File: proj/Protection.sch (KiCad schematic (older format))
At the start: 18 parts

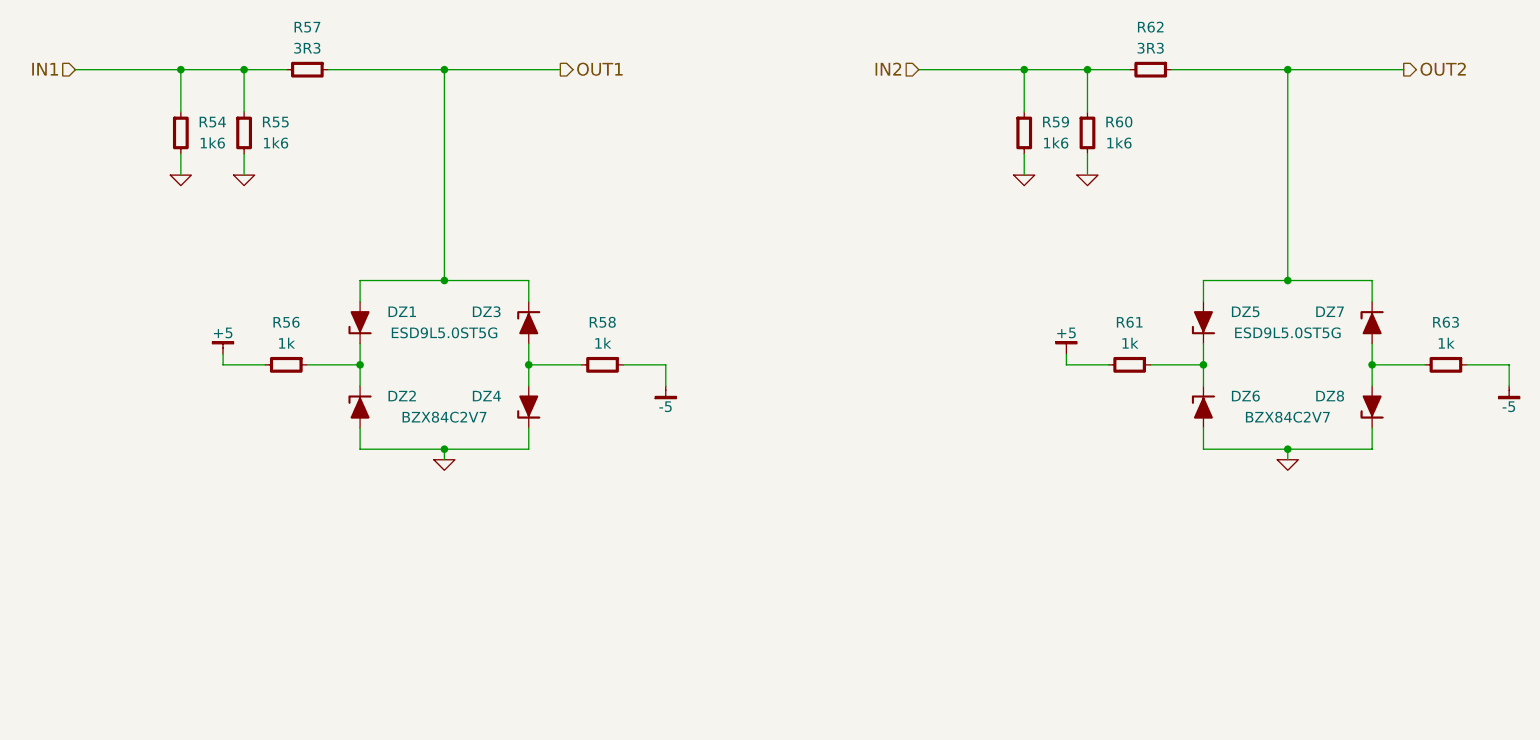
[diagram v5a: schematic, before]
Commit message: Clean up resistor BOM
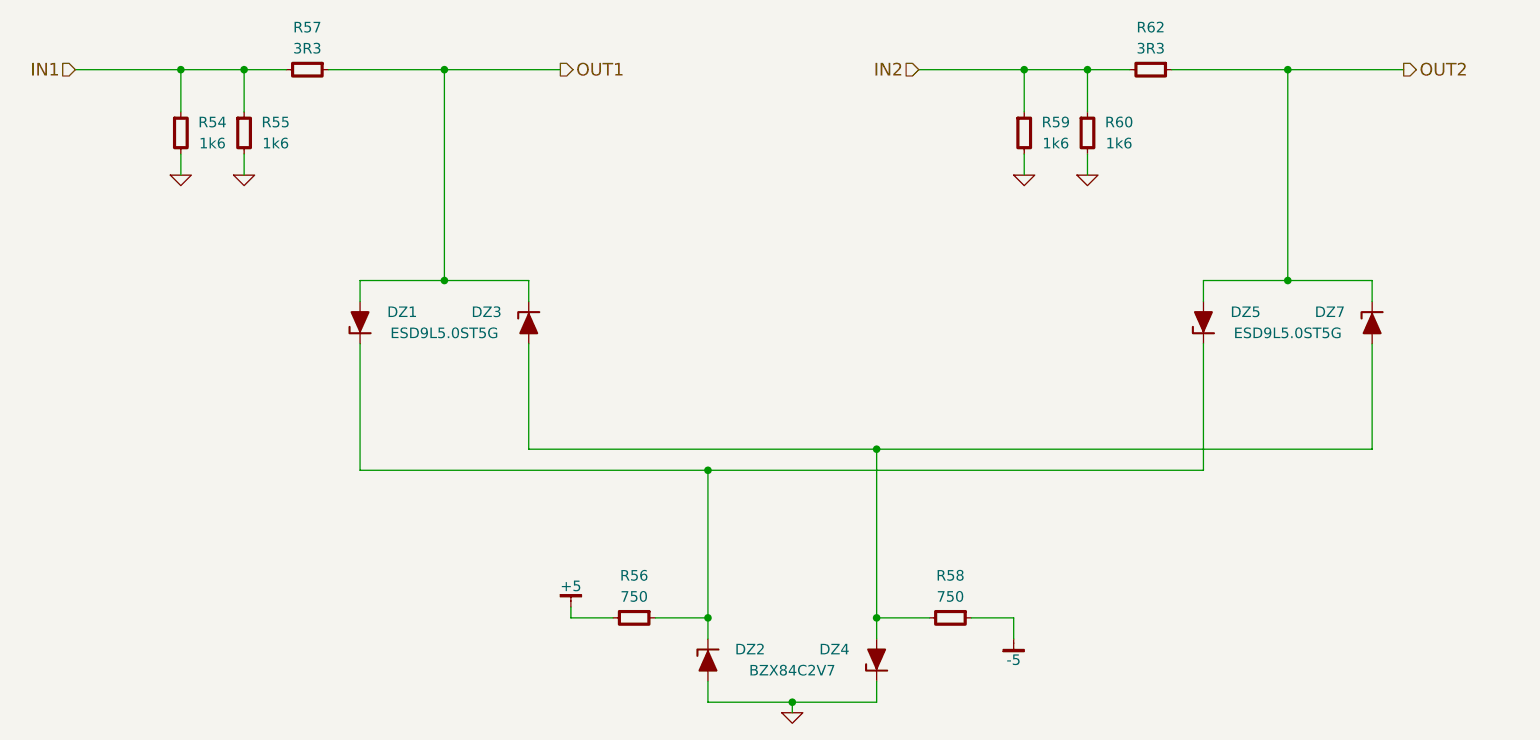
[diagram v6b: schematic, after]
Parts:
- removed DZ6, DZ8: BZX84C2V7, smd-semi:SOT-23, symbol BZX84
- removed R61, R63: 1k, IPC7351-Nominal:RESC1005X40, symbol R-0402
- R56, R58: value 1k -> 750; BOM RES SMD 1k 5% [0402] -> RES SMD 750 5% [0402]
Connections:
- net at DZ1.1, DZ2.3, R56.1: now also DZ5.1
- net at DZ3.2, DZ4.1, R58.2: now also DZ7.2
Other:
- moved on the sheet: DZ2, DZ4, R56, R58

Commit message: Swap 0402 to 0603, add USB inrush protection
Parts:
- removed R54, R55, R59, R60: 1k6, IPC7351-Nominal:RESC1005X40, symbol R-0402
- removed R57, R62: 3R3, IPC7351-Nominal:RESC1005X40, symbol R-0402
- added R54, R55, R59, R60: 1k6, IPC7351-Nominal:RESC1608X50, symbol R-0603
- added R57, R62: 3R3, IPC7351-Nominal:RESC1608X50, symbol R-0603
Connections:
- net GND: now also R54.2, R55.2, R59.2, R60.2
- net IN1: now also R54.1, R55.1, R57.2
- net IN2: now also R59.1, R60.1, R62.2
- net OUT1: now also R57.1
- net OUT2: now also R62.1
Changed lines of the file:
@@
 Wire Wire Line
 	2400 2300 3400 2300
-$Comp
-L R-0402 R54
-U 1 1 54F30EB5
-P 2900 2600
-F 0 "R54" H 3050 2650 50  0000 C CNN
-F 1 "1k6" H 3050 2550 50  0000 C CNN
-F 2 "IPC7351-Nominal:RESC1005X40" H 2900 2600 50  0001 C CNN
-F 3 "" H 2900 2650 60  0000 C CNN
-F 4 "Value" H 2900 2600 60  0001 C CNN "Manuf"
-F 5 "RES SMD 1.6k 1% [0402]" H 3650 3150 60  0001 C CNN "BOM"
-	1    2900 2600
-	1    0    0    -1
-$EndComp
-$Comp
-L R-0402 R55
-U 1 1 54F30F49
-P 3200 2600
-F 0 "R55" H 3350 2650 50  0000 C CNN
-F 1 "1k6" H 3350 2550 50  0000 C CNN
-F 2 "IPC7351-Nominal:RESC1005X40" H 3200 2600 50  0001 C CNN
-F 3 "" H 3200 2650 60  0000 C CNN
-F 4 "Value" H 3200 2600 60  0001 C CNN "Manuf"
-F 5 "RES SMD 1.6k 1% [0402]" H 3950 3150 60  0001 C CNN "BOM"
-	1    3200 2600
-	1    0    0    -1
-$EndComp
 Wire Wire Line
 	2900 2300 2900 2500
@@
 Connection ~ 2900 2300
 $Comp
-L GND #PWR0163
+L GND #PWR0156
 U 1 1 54F30F78
 P 2900 2800
-F 0 "#PWR0163" H 2900 2800 30  0001 C CNN
+F 0 "#PWR0156" H 2900 2800 30  0001 C CNN
 F 1 "GND" H 2900 2730 30  0001 C CNN
 F 2 "" H 2900 2800 60  0000 C CNN
@@
 	2900 2800 2900 2700
 $Comp
-L GND #PWR0164
+L GND #PWR0157
 U 1 1 54F30F98
 P 3200 2800
-F 0 "#PWR0164" H 3200 2800 30  0001 C CNN
+F 0 "#PWR0157" H 3200 2800 30  0001 C CNN
 F 1 "GND" H 3200 2730 30  0001 C CNN
 F 2 "" H 3200 2800 60  0000 C CNN
@@
 	3200 2800 3200 2700
 Connection ~ 3200 2300
-$Comp
-L R-0402 R57
-U 1 1 54F312FC
-P 3500 2300
-F 0 "R57" V 3300 2300 50  0000 C CNN
-F 1 "3R3" V 3400 2300 50  0000 C CNN
-F 2 "IPC7351-Nominal:RESC1005X40" H 3500 2300 50  0001 C CNN
-F 3 "" H 3500 2350 60  0000 C CNN
-F 4 "Value" H 3500 2300 60  0001 C CNN "Manuf"
-F 5 "RES SMD 3.3 5% [0402]" H 4250 2850 60  0001 C CNN "BOM"
-	1    3500 2300
-	0    1    1    0
-$EndComp
 $Comp
 L ESD9L DZ1
@@
 	6200 5300 6200 5200
 $Comp
-L GND #PWR0165
+L GND #PWR0158
 U 1 1 54F327AC
 P 5800 5350
-F 0 "#PWR0165" H 5800 5350 30  0001 C CNN
+F 0 "#PWR0158" H 5800 5350 30  0001 C CNN
 F 1 "GND" H 5800 5280 30  0001 C CNN
 F 2 "" H 5800 5350 60  0000 C CNN
@@
 Connection ~ 5400 4900
 $Comp
-L +5 #PWR0166
+L +5 #PWR0159
 U 1 1 54F328CE
 P 4750 4850
-F 0 "#PWR0166" H 4750 4900 30  0001 C CNN
+F 0 "#PWR0159" H 4750 4900 30  0001 C CNN
 F 1 "+5" H 4750 4950 50  0000 C CNN
 F 2 "" H 4750 4850 60  0000 C CNN
@@
 Connection ~ 6200 4900
 $Comp
-L -5 #PWR0167
+L -5 #PWR0160
 U 1 1 54F329A1
 P 6850 5000
-F 0 "#PWR0167" H 6850 4950 30  0001 C CNN
+F 0 "#PWR0160" H 6850 4950 30  0001 C CNN
 F 1 "-5" H 6850 4900 50  0000 C CNN
 F 2 "" H 6850 5000 60  0000 C CNN
@@
 Wire Wire Line
 	6400 2300 7400 2300
-$Comp
-L R-0402 R59
-U 1 1 54F32BFC
-P 6900 2600
-F 0 "R59" H 7050 2650 50  0000 C CNN
-F 1 "1k6" H 7050 2550 50  0000 C CNN
-F 2 "IPC7351-Nominal:RESC1005X40" H 6900 2600 50  0001 C CNN
-F 3 "" H 6900 2650 60  0000 C CNN
-F 4 "Value" H 6900 2600 60  0001 C CNN "Manuf"
-F 5 "RES SMD 1.6k 1% [0402]" H 7650 3150 60  0001 C CNN "BOM"
-	1    6900 2600
-	1    0    0    -1
-$EndComp
-$Comp
-L R-0402 R60
-U 1 1 54F32C04
-P 7200 2600
-F 0 "R60" H 7350 2650 50  0000 C CNN
-F 1 "1k6" H 7350 2550 50  0000 C CNN
-F 2 "IPC7351-Nominal:RESC1005X40" H 7200 2600 50  0001 C CNN
-F 3 "" H 7200 2650 60  0000 C CNN
-F 4 "Value" H 7200 2600 60  0001 C CNN "Manuf"
-F 5 "RES SMD 1.6k 1% [0402]" H 7950 3150 60  0001 C CNN "BOM"
-	1    7200 2600
-	1    0    0    -1
-$EndComp
 Wire Wire Line
 	6900 2300 6900 2500
@@
 Connection ~ 6900 2300
 $Comp
-L GND #PWR0168
+L GND #PWR0161
 U 1 1 54F32C0D
 P 6900 2800
-F 0 "#PWR0168" H 6900 2800 30  0001 C CNN
+F 0 "#PWR0161" H 6900 2800 30  0001 C CNN
 F 1 "GND" H 6900 2730 30  0001 C CNN
 F 2 "" H 6900 2800 60  0000 C CNN
@@
 	6900 2800 6900 2700
 $Comp
-L GND #PWR0169
+L GND #PWR0162
 U 1 1 54F32C14
 P 7200 2800
-F 0 "#PWR0169" H 7200 2800 30  0001 C CNN
+F 0 "#PWR0162" H 7200 2800 30  0001 C CNN
 F 1 "GND" H 7200 2730 30  0001 C CNN
 F 2 "" H 7200 2800 60  0000 C CNN
@@
 	7200 2800 7200 2700
 Connection ~ 7200 2300
-$Comp
-L R-0402 R62
-U 1 1 54F32C1E
-P 7500 2300
-F 0 "R62" V 7300 2300 50  0000 C CNN
-F 1 "3R3" V 7400 2300 50  0000 C CNN
-F 2 "IPC7351-Nominal:RESC1005X40" H 7500 2300 50  0001 C CNN
-F 3 "" H 7500 2350 60  0000 C CNN
-F 4 "Value" H 7500 2300 60  0001 C CNN "Manuf"
-F 5 "RES SMD 3.3 5% [0402]" H 8250 2850 60  0001 C CNN "BOM"
-	1    7500 2300
-	0    1    1    0
-$EndComp
 $Comp
 L ESD9L DZ5
@@
 	8550 4100 8550 3600
 Connection ~ 6200 4100
+$Comp
+L R-0603 R54
+U 1 1 5503F4A5
+P 2900 2600
+F 0 "R54" H 3050 2650 50  0000 C CNN
+F 1 "1k6" H 3050 2550 50  0000 C CNN
+F 2 "IPC7351-Nominal:RESC1608X50" H 2900 2600 50  0001 C CNN
+F 3 "" H 2900 2650 60  0000 C CNN
+F 4 "Value" H 2900 2600 60  0001 C CNN "Manuf"
+F 5 "RES SMD 1.6k 1% [0603]" H 3650 3150 60  0001 C CNN "BOM"
+	1    2900 2600
+	1    0    0    -1
+$EndComp
+$Comp
+L R-0603 R55
+U 1 1 5503F6C4
+P 3200 2600
+F 0 "R55" H 3350 2650 50  0000 C CNN
+F 1 "1k6" H 3350 2550 50  0000 C CNN
+F 2 "IPC7351-Nominal:RESC1608X50" H 3200 2600 50  0001 C CNN
+F 3 "" H 3200 2650 60  0000 C CNN
+F 4 "Value" H 3200 2600 60  0001 C CNN "Manuf"
+F 5 "RES SMD 1.6k 1% [0603]" H 3950 3150 60  0001 C CNN "BOM"
+	1    3200 2600
+	1    0    0    -1
+$EndComp
+$Comp
+L R-0603 R59
+U 1 1 5503F702
+P 6900 2600
+F 0 "R59" H 7050 2650 50  0000 C CNN
+F 1 "1k6" H 7050 2550 50  0000 C CNN
+F 2 "IPC7351-Nominal:RESC1608X50" H 6900 2600 50  0001 C CNN
+F 3 "" H 6900 2650 60  0000 C CNN
+F 4 "Value" H 6900 2600 60  0001 C CNN "Manuf"
+F 5 "RES SMD 1.6k 1% [0603]" H 7650 3150 60  0001 C CNN "BOM"
+	1    6900 2600
+	1    0    0    -1
+$EndComp
+$Comp
+L R-0603 R60
+U 1 1 5503F89E
+P 7200 2600
+F 0 "R60" H 7350 2650 50  0000 C CNN
+F 1 "1k6" H 7350 2550 50  0000 C CNN
+F 2 "IPC7351-Nominal:RESC1608X50" H 7200 2600 50  0001 C CNN
+F 3 "" H 7200 2650 60  0000 C CNN
+F 4 "Value" H 7200 2600 60  0001 C CNN "Manuf"
+F 5 "RES SMD 1.6k 1% [0603]" H 7950 3150 60  0001 C CNN "BOM"
+	1    7200 2600
+	1    0    0    -1
+$EndComp
+$Comp
+L R-0603 R57
+U 1 1 55041575
+P 3500 2300
+F 0 "R57" V 3300 2300 50  0000 C CNN
+F 1 "3R3" V 3400 2300 50  0000 C CNN
+F 2 "IPC7351-Nominal:RESC1608X50" H 3500 2300 50  0001 C CNN
+F 3 "" H 3500 2350 60  0000 C CNN
+F 4 "Value" H 3500 2300 60  0001 C CNN "Manuf"
+F 5 "RES SMD 3.3 5% [0603]" H 4250 2850 60  0001 C CNN "BOM"
+	1    3500 2300
+	0    1    1    0
+$EndComp
+$Comp
+L R-0603 R62
+U 1 1 5504172F
+P 7500 2300
+F 0 "R62" V 7300 2300 50  0000 C CNN
+F 1 "3R3" V 7400 2300 50  0000 C CNN
+F 2 "IPC7351-Nominal:RESC1608X50" H 7500 2300 50  0001 C CNN
+F 3 "" H 7500 2350 60  0000 C CNN
+F 4 "Value" H 7500 2300 60  0001 C CNN "Manuf"
+F 5 "RES SMD 3.3 5% [0603]" H 8250 2850 60  0001 C CNN "BOM"
+	1    7500 2300
+	0    1    1    0
+$EndComp
 $EndSCHEMATC

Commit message: Touch up PCB
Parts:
- removed R56, R58: 750, IPC7351-Nominal:RESC1005X40, symbol R-0402
- added R56, R58: 750, IPC7351-Nominal:RESC1608X50, symbol R-0603
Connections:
- net +5: now also R56.2
- net -5: now also R58.1
- net at DZ1.1, DZ2.3, DZ5.1: now also R56.1
- net at DZ3.2, DZ4.1, DZ7.2: now also R58.2
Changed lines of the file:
@@
 	5800 5350 5800 5300
 Connection ~ 5800 5300
-$Comp
-L R-0402 R56
-U 1 1 54F327E4
-P 5050 4900
-F 0 "R56" V 4850 4900 50  0000 C CNN
-F 1 "750" V 4950 4900 50  0000 C CNN
-F 2 "IPC7351-Nominal:RESC1005X40" H 5050 4900 50  0001 C CNN
-F 3 "" H 5050 4950 60  0000 C CNN
-F 4 "Value" H 5050 4900 60  0001 C CNN "Manuf"
-F 5 "RES SMD 750 5% [0402]" H 5800 5450 60  0001 C CNN "BOM"
-	1    5050 4900
-	0    1    1    0
-$EndComp
 Wire Wire Line
 	5150 4900 5400 4900
@@
 Wire Wire Line
 	4750 4900 4950 4900
-$Comp
-L R-0402 R58
-U 1 1 54F3293C
-P 6550 4900
-F 0 "R58" V 6350 4900 50  0000 C CNN
-F 1 "750" V 6450 4900 50  0000 C CNN
-F 2 "IPC7351-Nominal:RESC1005X40" H 6550 4900 50  0001 C CNN
-F 3 "" H 6550 4950 60  0000 C CNN
-F 4 "Value" H 6550 4900 60  0001 C CNN "Manuf"
-F 5 "RES SMD 750 5% [0402]" H 7300 5450 60  0001 C CNN "BOM"
-	1    6550 4900
-	0    1    1    0
-$EndComp
 Wire Wire Line
 	6450 4900 6200 4900
@@
 	0    1    1    0
 $EndComp
+$Comp
+L R-0603 R56
+U 1 1 54FE871D
+P 5050 4900
+F 0 "R56" V 4850 4900 50  0000 C CNN
+F 1 "750" V 4950 4900 50  0000 C CNN
+F 2 "IPC7351-Nominal:RESC1608X50" H 5050 4900 50  0001 C CNN
+F 3 "" H 5050 4950 60  0000 C CNN
+F 4 "Value" H 5050 4900 60  0001 C CNN "Manuf"
+F 5 "RES SMD 750 1% [0603]" H 5800 5450 60  0001 C CNN "BOM"
+	1    5050 4900
+	0    1    1    0
+$EndComp
+$Comp
+L R-0603 R58
+U 1 1 54FE88AB
+P 6550 4900
+F 0 "R58" V 6350 4900 50  0000 C CNN
+F 1 "750" V 6450 4900 50  0000 C CNN
+F 2 "IPC7351-Nominal:RESC1608X50" H 6550 4900 50  0001 C CNN
+F 3 "" H 6550 4950 60  0000 C CNN
+F 4 "Value" H 6550 4900 60  0001 C CNN "Manuf"
+F 5 "RES SMD 750 1% [0603]" H 7300 5450 60  0001 C CNN "BOM"
+	1    6550 4900
+	0    1    1    0
+$EndComp
